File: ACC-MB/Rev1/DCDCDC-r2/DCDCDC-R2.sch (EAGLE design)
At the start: 21 parts, among them X2 5566-4

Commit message: update
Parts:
- U$8: value 600W 400 to 12V -> VICOR_CHIP_WITH_HEATSINK
- renumbered DCM290P138T600A40 to U$8
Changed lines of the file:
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@@
 <parts>
 <part name="FRAME1" library="ACC-MB-R0" library_urn="urn:adsk.eagle:library:13324935" deviceset="A3L-LOC" device=""/>
-<part name="DCM290P138T600A40" library="ACC-MB-R0" library_urn="urn:adsk.eagle:library:13324935" deviceset="VICOR_CHIP_WITH_HEATSINK" device="" package3d_urn="urn:adsk.eagle:package:13209498/1" value="600W 400 to 12V"/>
 <part name="P+2" library="ACC-MB-R0" library_urn="urn:adsk.eagle:library:13324935" deviceset="V+" device=""/>
 <part name="P-1" library="ACC-MB-R0" library_urn="urn:adsk.eagle:library:13324935" deviceset="V-" device=""/>
@@
 <part name="P+5" library="ACC-MB-R0" library_urn="urn:adsk.eagle:library:13208985" deviceset="+12V" device=""/>
 <part name="GND1" library="ACC-MB-R0" library_urn="urn:adsk.eagle:library:13208985" deviceset="GND" device=""/>
+<part name="U$8" library="ACC-MB-R0" library_urn="urn:adsk.eagle:library:13208985" deviceset="VICOR_CHIP_WITH_HEATSINK" device="" package3d_urn="urn:adsk.eagle:package:13209498/2"/>
 </parts>
 <sheets>
@@
 <attribute name="SHEET" x="357.505" y="5.08" size="2.54" layer="94"/>
 </instance>
-<instance part="DCM290P138T600A40" gate="G$1" x="105.41" y="219.71" smashed="yes" rot="R270">
-<attribute name="VALUE" x="111.252" y="217.424" size="1.27" layer="96" rot="R270"/>
-<attribute name="NAME" x="113.03" y="219.71" size="1.27" layer="95" rot="R270"/>
-</instance>
 <instance part="P+2" gate="1" x="27.94" y="229.87" smashed="yes">
 <attribute name="VALUE" x="25.4" y="227.33" size="1.778" layer="96" rot="R90"/>
@@
 <instance part="P+5" gate="1" x="19.05" y="139.7"/>
 <instance part="GND1" gate="1" x="19.05" y="107.95"/>
+<instance part="U$8" gate="G$1" x="105.41" y="219.71" rot="R270"/>
 </instances>
 <busses>
@@
 </segment>
 <segment>
-<pinref part="DCM290P138T600A40" gate="G$1" pin="OUT-_1"/>
 <wire x1="130.81" y1="214.63" x2="143.51" y2="214.63" width="0.1524" layer="91"/>
 <wire x1="143.51" y1="214.63" x2="143.51" y2="201.93" width="0.1524" layer="91"/>
-<pinref part="DCM290P138T600A40" gate="G$1" pin="OUT-_2"/>
 <wire x1="143.51" y1="201.93" x2="143.51" y2="195.58" width="0.1524" layer="91"/>
 <wire x1="143.51" y1="195.58" x2="143.51" y2="193.04" width="0.1524" layer="91"/>
@@
 <wire x1="162.56" y1="195.58" x2="143.51" y2="195.58" width="0.1524" layer="91"/>
 <junction x="143.51" y="195.58"/>
+<pinref part="U$8" gate="G$1" pin="OUT-_1"/>
+<pinref part="U$8" gate="G$1" pin="OUT-_2"/>
 </segment>
 <segment>
@@
 <pinref part="CFILTER_2" gate="G$1" pin="2"/>
 <wire x1="95.25" y1="209.55" x2="95.25" y2="196.85" width="0.1524" layer="91"/>
-<pinref part="DCM290P138T600A40" gate="G$1" pin="IN-"/>
 <wire x1="100.33" y1="201.93" x2="99.06" y2="201.93" width="0.1524" layer="91"/>
 <wire x1="99.06" y1="201.93" x2="99.06" y2="196.85" width="0.1524" layer="91"/>
 <wire x1="99.06" y1="196.85" x2="95.25" y2="196.85" width="0.1524" layer="91"/>
 <junction x="95.25" y="196.85"/>
+<pinref part="U$8" gate="G$1" pin="IN-"/>
 </segment>
 <segment>
@@
 <segment>
 <pinref part="L_IN" gate="G$1" pin="2"/>
-<pinref part="DCM290P138T600A40" gate="G$1" pin="IN+"/>
 <wire x1="78.74" y1="219.71" x2="86.36" y2="219.71" width="0.1524" layer="91"/>
 <pinref part="CFILTER_1" gate="G$1" pin="1"/>
@@
 <wire x1="76.2" y1="231.14" x2="86.36" y2="231.14" width="0.1524" layer="91"/>
 <wire x1="86.36" y1="231.14" x2="86.36" y2="219.71" width="0.1524" layer="91"/>
+<pinref part="U$8" gate="G$1" pin="IN+"/>
 </segment>
 </net>
@@
 <net name="DCDC_OUT" class="1">
 <segment>
-<pinref part="DCM290P138T600A40" gate="G$1" pin="OUT+_1"/>
 <wire x1="130.81" y1="219.71" x2="162.56" y2="219.71" width="0.1524" layer="91"/>
-<pinref part="DCM290P138T600A40" gate="G$1" pin="OUT+_2"/>
 <wire x1="130.81" y1="207.01" x2="162.56" y2="207.01" width="0.1524" layer="91"/>
 <wire x1="162.56" y1="207.01" x2="162.56" y2="219.71" width="0.1524" layer="91"/>
@@
 <wire x1="162.56" y1="205.74" x2="162.56" y2="207.01" width="0.1524" layer="91"/>
 <junction x="162.56" y="207.01"/>
-</segment>
-<segment>
+<pinref part="U$8" gate="G$1" pin="OUT+_1"/>
+<pinref part="U$8" gate="G$1" pin="OUT+_2"/>
+</segment>
+<segment>

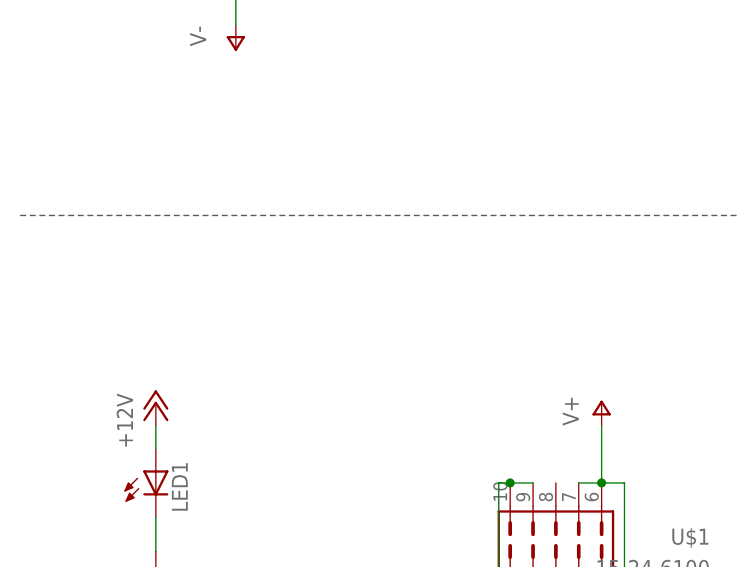
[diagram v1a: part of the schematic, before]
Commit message: 7792 added to all DC
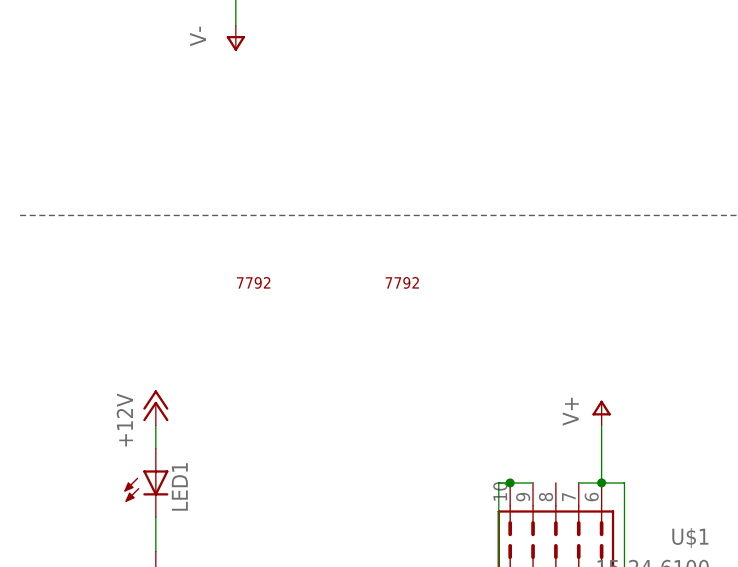
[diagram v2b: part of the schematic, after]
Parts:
- added U$10, U$9: 7792, ACC-MB-R0:7792
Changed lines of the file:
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@@
 <part name="GND1" library="ACC-MB-R0" library_urn="urn:adsk.eagle:library:13208985" deviceset="GND" device=""/>
 <part name="U$8" library="ACC-MB-R0" library_urn="urn:adsk.eagle:library:13208985" deviceset="VICOR_CHIP_WITH_HEATSINK" device="" package3d_urn="urn:adsk.eagle:package:13209498/2"/>
+<part name="U$9" library="ACC-MB-R0" library_urn="urn:adsk.eagle:library:13208985" deviceset="7792" device="" package3d_urn="urn:adsk.eagle:package:14511284/2"/>
+<part name="U$10" library="ACC-MB-R0" library_urn="urn:adsk.eagle:library:13208985" deviceset="7792" device="" package3d_urn="urn:adsk.eagle:package:14511284/2"/>
 </parts>
 <sheets>
@@
 <instance part="GND1" gate="1" x="19.05" y="107.95"/>
 <instance part="U$8" gate="G$1" x="105.41" y="219.71" rot="R270"/>
+<instance part="U$9" gate="G$1" x="27.94" y="152.4"/>
+<instance part="U$10" gate="G$1" x="44.45" y="152.4"/>
 </instances>
 <busses>
